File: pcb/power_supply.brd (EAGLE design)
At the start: 57.3 x 66.4 mm, 53 parts, among them CON1 +, CON2 +, CON3 +, CON4 +, CON5 +, CON6 +, CON7 +, CON8 +, IC1 AP1507-D5-13, P1 2k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

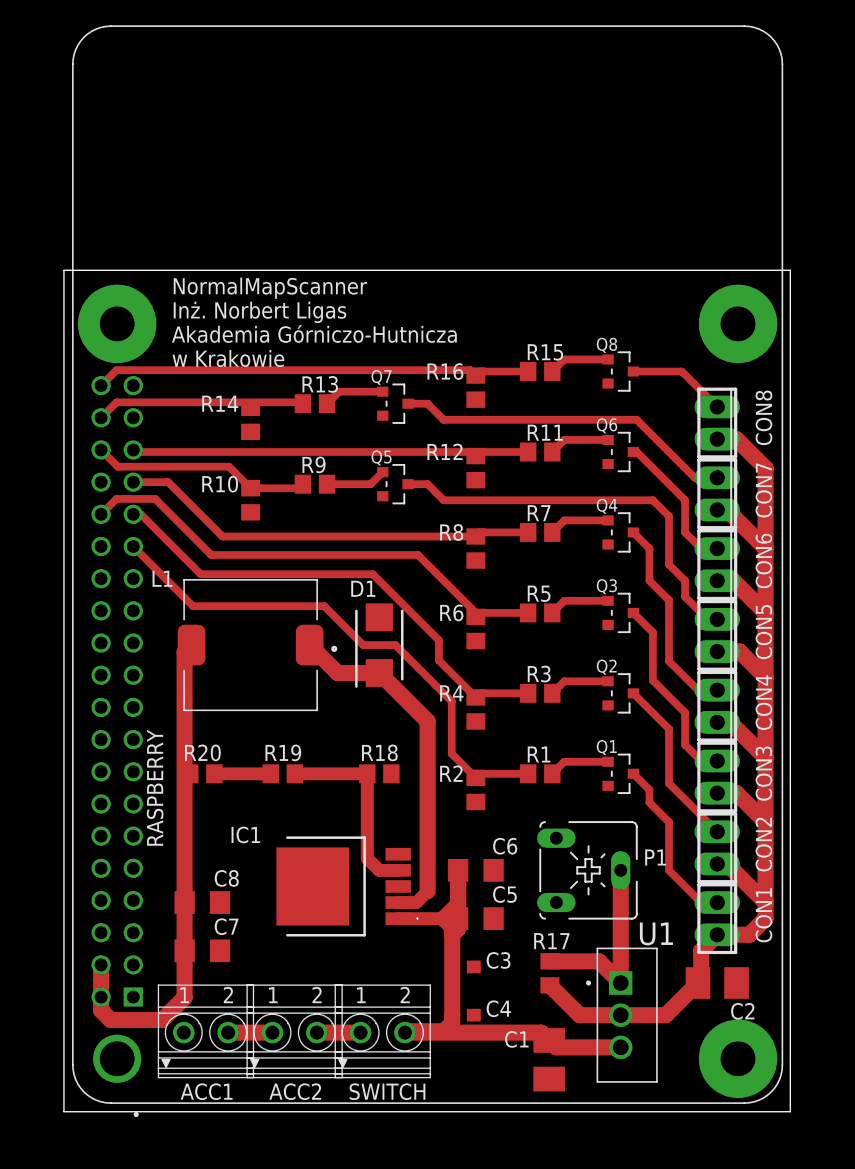
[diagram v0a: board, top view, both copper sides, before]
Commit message: pcb - GND top layer
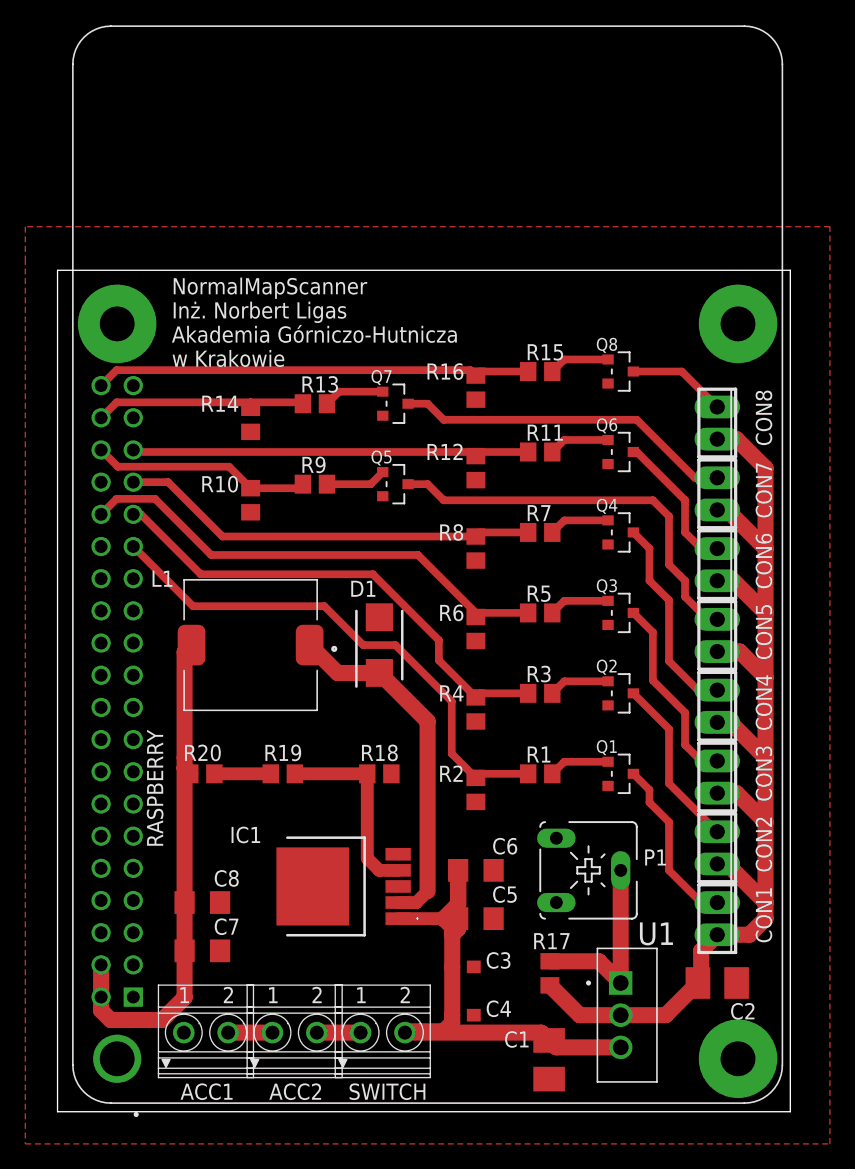
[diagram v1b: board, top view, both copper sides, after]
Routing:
- net RASP_SUPPLY: track 39.8 -> 40.4 mm
- added copper zone on layer 1, net GND
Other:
- board size 57.3 x 66.4 mm -> 57.8 x 66.4 mm
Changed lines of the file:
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@@
 <board>
 <plain>
-<wire x1="0.508" y1="1.27" x2="57.836" y2="1.27" width="0" layer="20"/>
+<wire x1="0" y1="1.27" x2="57.836" y2="1.27" width="0" layer="20"/>
 <wire x1="57.836" y1="1.27" x2="57.836" y2="67.681" width="0" layer="20"/>
-<wire x1="57.836" y1="67.681" x2="0.508" y2="67.681" width="0" layer="20"/>
-<wire x1="0.508" y1="67.681" x2="0.508" y2="1.27" width="0" layer="20"/>
+<wire x1="57.836" y1="67.681" x2="0" y2="67.681" width="0" layer="20"/>
+<wire x1="0" y1="67.681" x2="0" y2="1.27" width="0" layer="20"/>
 <text x="9.017" y="60.071" size="1.27" layer="25">NormalMapScanner
 Inż. Norbert Ligas
@@
 <contactref element="Q8" pad="2"/>
 <contactref element="ACC1" pad="1"/>
-<wire x1="43.45" y1="58.74" x2="53.71" y2="63.45" width="0" layer="19" extent="1-1"/>
-<wire x1="43.45" y1="52.39" x2="43.45" y2="58.74" width="0" layer="19" extent="1-1"/>
-<wire x1="43.45" y1="46.04" x2="43.45" y2="52.39" width="0" layer="19" extent="1-1"/>
-<wire x1="43.45" y1="39.69" x2="43.45" y2="46.04" width="0" layer="19" extent="1-1"/>
-<wire x1="43.45" y1="33.34" x2="43.45" y2="39.69" width="0" layer="19" extent="1-1"/>
-<wire x1="43.45" y1="26.99" x2="43.45" y2="33.34" width="0" layer="19" extent="1-1"/>
-<wire x1="39.37" y1="22.86" x2="43.45" y2="26.99" width="0" layer="19" extent="1-1"/>
-<wire x1="34.42" y1="20.32" x2="39.37" y2="22.86" width="0" layer="19" extent="1-1"/>
-<wire x1="34.42" y1="16.51" x2="34.42" y2="20.32" width="0" layer="19" extent="1-1"/>
-<wire x1="32.854" y1="12.7" x2="34.42" y2="16.51" width="0" layer="19" extent="1-1"/>
-<wire x1="32.854" y1="8.89" x2="32.854" y2="12.7" width="0" layer="19" extent="1-1"/>
-<wire x1="33.02" y1="25.72" x2="34.42" y2="20.32" width="0" layer="19" extent="1-1"/>
-<wire x1="33.02" y1="32.07" x2="33.02" y2="25.72" width="0" layer="19" extent="1-1"/>
-<wire x1="33.02" y1="38.42" x2="33.02" y2="32.07" width="0" layer="19" extent="1-1"/>
-<wire x1="33.02" y1="44.77" x2="33.02" y2="38.42" width="0" layer="19" extent="1-1"/>
-<wire x1="33.02" y1="51.12" x2="33.02" y2="44.77" width="0" layer="19" extent="1-1"/>
-<wire x1="33.02" y1="57.47" x2="33.02" y2="51.12" width="0" layer="19" extent="1-1"/>
-<wire x1="26.35" y1="27.94" x2="33.02" y2="25.72" width="0" layer="19" extent="1-1"/>
-<wire x1="26.885" y1="21.59" x2="26.35" y2="27.94" width="0" layer="19" extent="1-1"/>
-<wire x1="26.885" y1="19.05" x2="26.885" y2="21.59" width="0" layer="19" extent="1-1"/>
-<wire x1="20.14" y1="19.05" x2="26.885" y2="19.05" width="0" layer="19" extent="1-1"/>
-<wire x1="12.83" y1="17.78" x2="20.14" y2="19.05" width="0" layer="19" extent="1-1"/>
-<wire x1="12.83" y1="13.97" x2="12.83" y2="17.78" width="0" layer="19" extent="1-1"/>
-<wire x1="9.9657" y1="7.5138" x2="12.83" y2="13.97" width="0" layer="19" extent="1-1"/>
-<wire x1="4.71" y1="5.45" x2="9.9657" y2="7.5138" width="0" layer="19" extent="1-1"/>
-<wire x1="5.98" y1="20.48" x2="12.83" y2="17.78" width="0" layer="19" extent="1-1"/>
-<wire x1="3.44" y1="25.56" x2="5.98" y2="20.48" width="0" layer="19" extent="1-1"/>
-<wire x1="3.44" y1="15.4" x2="5.98" y2="20.48" width="0" layer="19" extent="1-1"/>
-<wire x1="25.67" y1="56.2" x2="33.02" y2="57.47" width="0" layer="19" extent="1-1"/>
-<wire x1="25.67" y1="49.85" x2="25.67" y2="56.2" width="0" layer="19" extent="1-1"/>
-<wire x1="3.44" y1="33.18" x2="3.44" y2="25.56" width="0" layer="19" extent="1-1"/>
-<wire x1="38.7985" y1="3.8471" x2="32.854" y2="8.89" width="0" layer="19" extent="1-1"/>
-<wire x1="25.4" y1="40.3" x2="33.02" y2="38.42" width="0" layer="19" extent="1-1"/>
-<wire x1="5.98" y1="40.8" x2="3.44" y2="33.18" width="0" layer="19" extent="1-1"/>
-<wire x1="3.44" y1="45.88" x2="5.98" y2="40.8" width="0" layer="19" extent="1-1"/>
-<wire x1="3.44" y1="50.96" x2="3.44" y2="45.88" width="0" layer="19" extent="1-1"/>
-<wire x1="5.98" y1="58.58" x2="3.44" y2="50.96" width="0" layer="19" extent="1-1"/>
-<wire x1="4.71" y1="63.45" x2="5.98" y2="58.58" width="0" layer="19" extent="1-1"/>
-<wire x1="15.24" y1="54.93" x2="5.98" y2="58.58" width="0" layer="19" extent="1-1"/>
-<wire x1="15.24" y1="48.58" x2="15.24" y2="54.93" width="0" layer="19" extent="1-1"/>
-<wire x1="53.71" y1="5.45" x2="38.7985" y2="3.8471" width="0" layer="19" extent="1-1"/>
-<wire x1="53.595" y1="11.43" x2="53.71" y2="5.45" width="0" layer="19" extent="1-1"/>
+<polygon width="0.1524" layer="1">
+<vertex x="-2.54" y="68.58"/>
+<vertex x="-2.54" y="-1.27"/>
+<vertex x="60.96" y="-1.27"/>
+<vertex x="60.96" y="71.12"/>
+<vertex x="-2.54" y="71.12"/>
+</polygon>
 </signal>
 <signal name="BAT">
@@
 <wire x1="30.48" y1="7.62" x2="31.154" y2="8.294" width="1.27" layer="1"/>
 <wire x1="31.154" y1="8.294" x2="31.154" y2="8.89" width="1.27" layer="1"/>
-<wire x1="31.154" y1="8.89" x2="31.154" y2="15.24" width="1.27" layer="1"/>
+<wire x1="31.154" y1="8.89" x2="31.154" y2="12.7" width="1.27" layer="1"/>
 <wire x1="31.154" y1="15.24" x2="31.154" y2="15.836" width="1.27" layer="1"/>
 <wire x1="30.4974" y1="16.4926" x2="31.154" y2="15.836" width="1.27" layer="1"/>
@@
 <wire x1="26.885" y1="16.51" x2="30.48" y2="16.51" width="1.016" layer="1"/>
 <wire x1="30.48" y1="16.51" x2="30.4974" y2="16.4926" width="1.016" layer="1"/>
-<wire x1="31.154" y1="8.89" x2="31.154" y2="12.7" width="0" layer="19" extent="1-1"/>
+<wire x1="31.154" y1="12.7" x2="31.154" y2="15.24" width="1.27" layer="1"/>
 </signal>
 <signal name="N$22">
@@
 <wire x1="5.98" y1="53.5" x2="6.19" y2="53.5" width="0.6096" layer="1"/>
 <wire x1="6.19" y1="53.5" x2="6.35" y2="53.34" width="0.6096" layer="1"/>
-<wire x1="6.35" y1="53.34" x2="37.15" y2="53.34" width="0.6096" layer="1"/>
-<wire x1="37.15" y1="53.34" x2="33.02" y2="53.02" width="0" layer="19" extent="1-1"/>
+<wire x1="6.35" y1="53.34" x2="33.02" y2="53.34" width="0.6096" layer="1"/>
+<wire x1="33.02" y1="53.34" x2="37.15" y2="53.34" width="0.6096" layer="1"/>
+<wire x1="33.02" y1="53.02" x2="33.02" y2="53.34" width="0.6096" layer="1"/>
 </signal>
 <signal name="N$26">
@@
 <wire x1="3.44" y1="56.04" x2="4.6592" y2="57.2592" width="0.6096" layer="1"/>
 <wire x1="15.24" y1="56.83" x2="15.56" y2="57.15" width="0.6096" layer="1"/>
+<wire x1="4.6592" y1="57.2592" x2="15.24" y2="57.2592" width="0.6096" layer="1"/>
+<wire x1="15.24" y1="57.2592" x2="19.2608" y2="57.2592" width="0.6096" layer="1"/>
 <wire x1="19.2608" y1="57.2592" x2="19.37" y2="57.15" width="0.6096" layer="1"/>
-<wire x1="4.6592" y1="57.2592" x2="19.2608" y2="57.2592" width="0.6096" layer="1"/>
-<wire x1="19.37" y1="57.15" x2="15.56" y2="57.15" width="0" layer="19" extent="1-1"/>
+<wire x1="15.24" y1="56.83" x2="15.24" y2="57.2592" width="0.6096" layer="1"/>
 </signal>
 <signal name="N$27">
@@
 <contactref element="C8" pad="1"/>
 <contactref element="R20" pad="1"/>
-<wire x1="10.58" y1="38.1" x2="10.03" y2="37.55" width="1.27" layer="1"/>
-<wire x1="10.03" y1="37.55" x2="10.03" y2="13.97" width="1.27" layer="1"/>
+<wire x1="10.03" y1="37.55" x2="10.03" y2="29.21" width="1.27" layer="1"/>
+<wire x1="10.03" y1="28.39" x2="10.03" y2="17.78" width="1.27" layer="1"/>
 <wire x1="10.03" y1="13.97" x2="10.03" y2="14.0792" width="0.6096" layer="1"/>
 <wire x1="3.80941875" y1="10.32" x2="3.44" y2="10.32" width="0.6096" layer="1"/>
 <wire x1="3.44" y1="10.32" x2="3.44" y2="9.26" width="1.27" layer="1"/>
 <wire x1="4.191" y1="8.509" x2="8.255" y2="8.509" width="1.27" layer="1"/>
-<wire x1="8.255" y1="8.509" x2="10.03" y2="10.284" width="1.27" layer="1"/>
-<wire x1="10.03" y1="10.284" x2="10.03" y2="13.97" width="1.27" layer="1"/>
+<wire x1="10.03" y1="10.284" x2="8.255" y2="8.509" width="1.27" layer="1"/>
 <wire x1="3.44" y1="9.26" x2="4.191" y2="8.509" width="1.27" layer="1"/>
 <wire x1="3.44" y1="10.32" x2="3.44" y2="12.86" width="1.27" layer="1"/>
-<wire x1="10.58" y1="38.1" x2="10.48" y2="27.94" width="0" layer="19" extent="1-1"/>
-<wire x1="10.03" y1="17.78" x2="10.03" y2="14.0792" width="0" layer="19" extent="1-1"/>
+<wire x1="10.03" y1="13.97" x2="10.03" y2="10.284" width="1.27" layer="1"/>
+<wire x1="10.03" y1="17.78" x2="10.03" y2="13.97" width="1.27" layer="1"/>
+<wire x1="10.58" y1="38.1" x2="10.03" y2="37.55" width="1.27" layer="1"/>
+<wire x1="10.48" y1="27.94" x2="10.03" y2="28.39" width="1.27" layer="1"/>
+<wire x1="10.03" y1="28.39" x2="10.03" y2="29.21" width="1.27" layer="1"/>
 </signal>
 <signal name="N$32">
@@
 <mfgpreviewcolor name="substratecolor" color="0xFF786E46"/>
 </mfgpreviewcolors>
+<errors>
+</errors>
 </board>
 </drawing>
